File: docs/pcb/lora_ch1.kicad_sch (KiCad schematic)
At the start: 6 parts, among them J1 JST_02, U1 ESP32-C3_SUPERMINI_TH, U2 TP4056-42-ESOP8, U3 DRV2605LDGS, U4 AP2112K-3.3

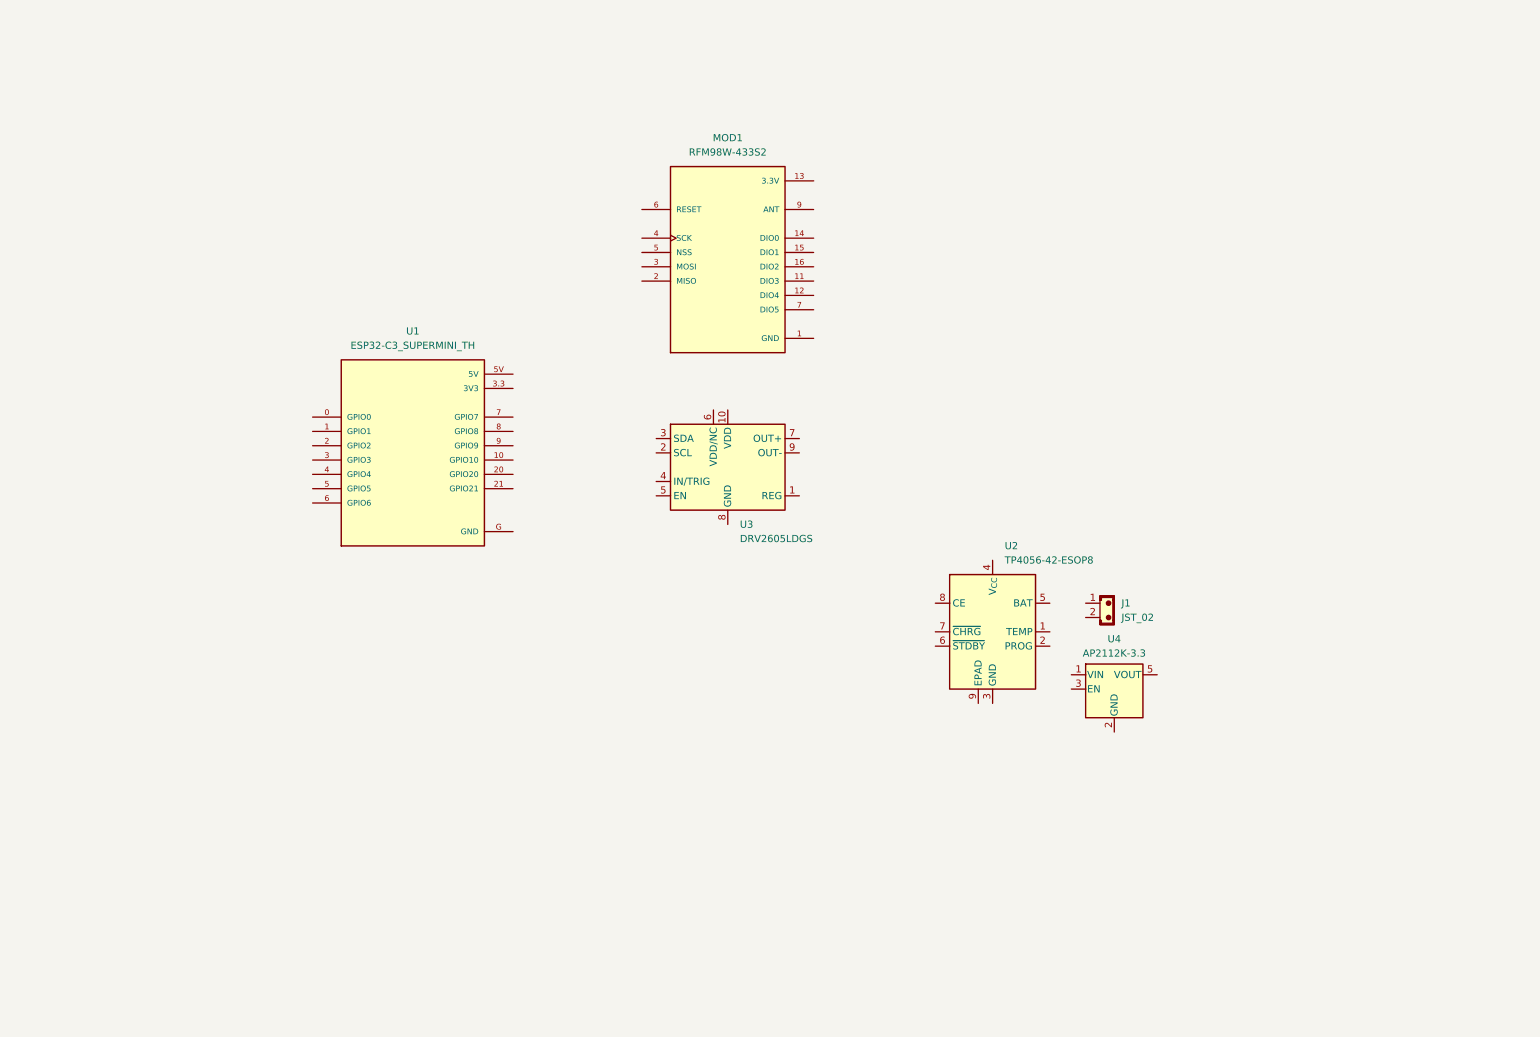
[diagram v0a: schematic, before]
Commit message: PCB schematic update, charging function added.
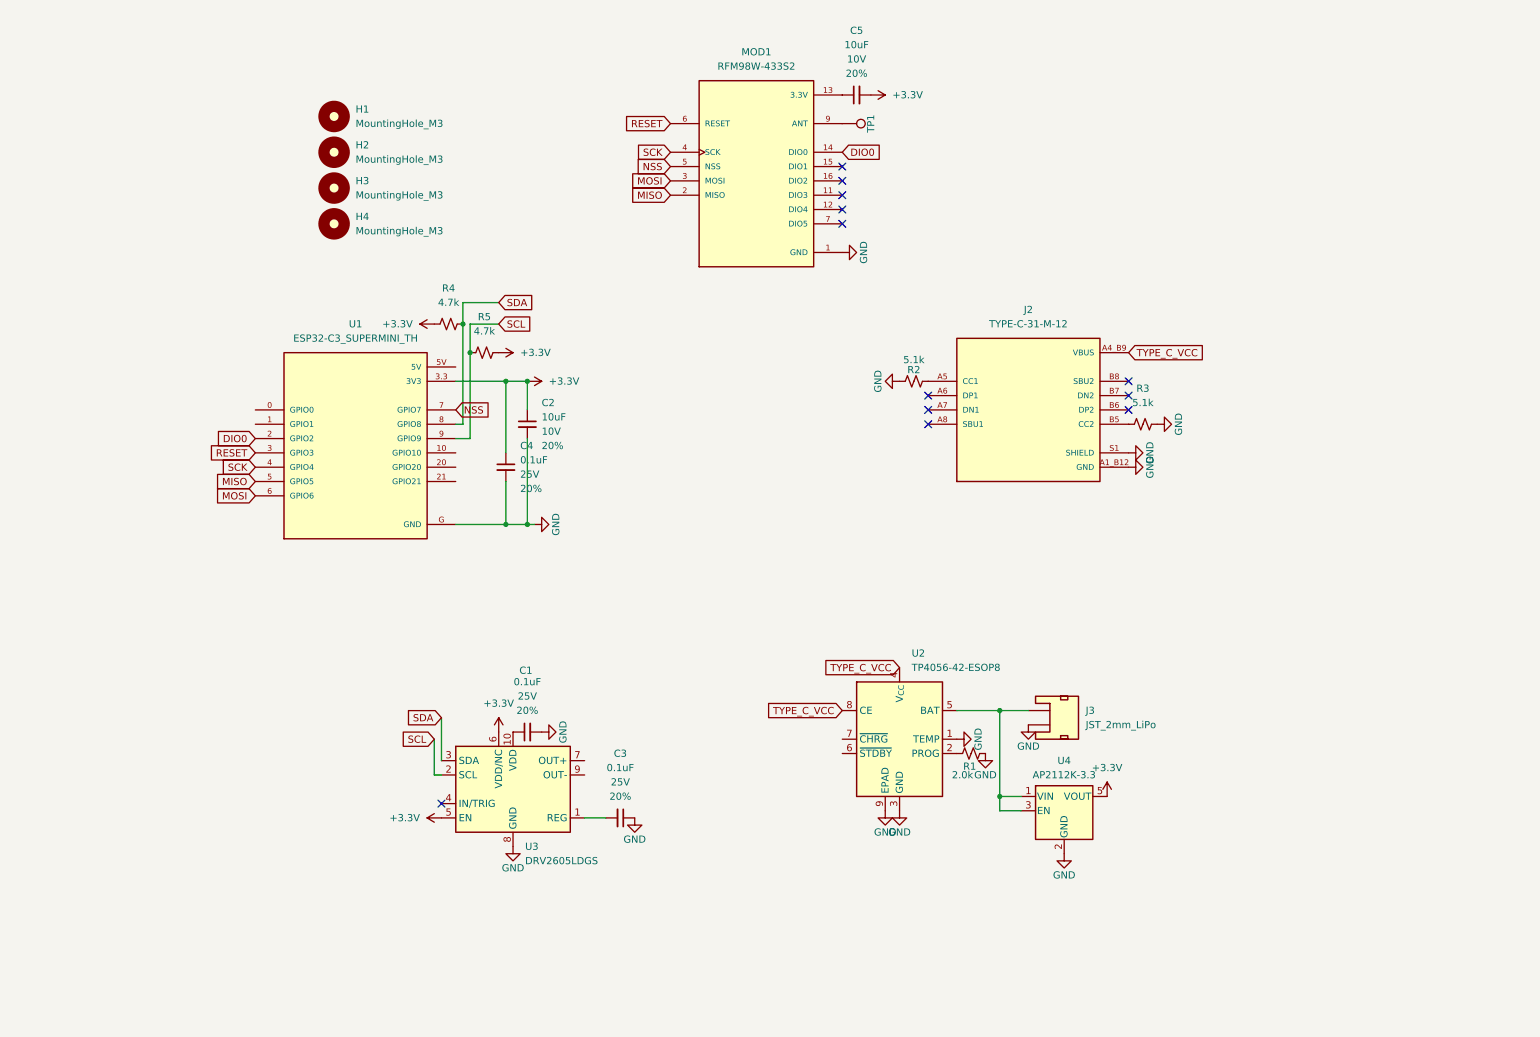
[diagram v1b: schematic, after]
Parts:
- removed J1: JST_02, Connector_JST:JST_EH_B2B-EH-A_1x02_P2.50mm_Vertical, symbol PCM_SL_Connectors:JST_02
- added C1, C3, C4: 0.1uF, PCM_SparkFun-Capacitor:C_0603_1608Metric, symbol PCM_SparkFun-Capacitor:0.1uF_0603_25V_20%
- added C2, C5: 10uF, PCM_SparkFun-Capacitor:C_0603_1608Metric, symbol PCM_SparkFun-Capacitor:10uF_0603_10V_20%
- added H1, H2, H3, H4: MountingHole_M3, MountingHole:MountingHole_3.2mm_M3, symbol PCM_SL_Mechanical:MountingHole_M3
- added J2: TYPE-C-31-M-12, TYPE-C-31-M-12:HRO_TYPE-C-31-M-12, symbol TYPE-C-31-M-12:TYPE-C-31-M-12
- added J3: JST_2mm_LiPo, PCM_SparkFun-Connector:JST_1x02_P2.0mm_Horizontal_SMD, symbol PCM_SparkFun-Connector:Conn_01x02_JST_P2.0mm_Horizontal_SMD
- added R1: 2.0k, PCM_SparkFun-Resistor:R_0603_1608Metric, symbol PCM_SparkFun-Resistor:2.0k_0603
- added R2, R3: 5.1k, PCM_SparkFun-Resistor:R_0603_1608Metric, symbol PCM_SparkFun-Resistor:5.1k_0603
- added R4, R5: 4.7k, PCM_SparkFun-Resistor:R_0603_1608Metric, symbol PCM_SparkFun-Resistor:4.7k_0603
- added TP1: 1.25mm, PCM_SparkFun-Connector:TestPoint-1.25mm, symbol PCM_SparkFun-Connector:TestPoint_1.25mm
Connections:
- net 3.3V: now also C5.1
- net GND: now also U1.G (GND), U2.1 (TEMP), U2.3 (GND), U2.9 (EPAD), U3.8 (GND), U4.2 (GND), C1.2, C2.2, C3.1, C4.2, J2.A1_B12 (GND), J2.B1_A12 (GND), J2.S1 (SHIELD), J2.S2 (SHIELD), J2.S3 (SHIELD), J2.S4 (SHIELD), J3.1 (-), R1.2, R2.1, R3.2
- net DIO0: now reaches MOD1.14 (DIO0), MOD1.14_1 (DIO0)
- net DIO0: now also U1.2 (GPIO2)
- net MISO: now reaches MOD1.2 (MISO), MOD1.2_1 (MISO)
- net MISO: now also U1.5 (GPIO5)
- net MOSI: now reaches MOD1.3 (MOSI), MOD1.3_1 (MOSI)
- net MOSI: now also U1.6 (GPIO6)
- net SCK: now reaches MOD1.4 (SCK), MOD1.4_1 (SCK)
- net SCK: now also U1.4 (GPIO4)
- net NSS: now reaches MOD1.5 (NSS), MOD1.5_1 (NSS)
- net NSS: now also U1.7 (GPIO7)
- net RESET: now reaches MOD1.6 (RESET), MOD1.6_1 (RESET)
- net RESET: now also U1.3 (GPIO3)
- net at MOD1.9 (ANT), MOD1.9_1 (ANT): now also TP1.1
- net at U4.1 (VIN): now also U2.5 (BAT), U4.3 (EN), J3.2 (+)
- net +3.3V: now reaches U4.5 (VOUT)
- net +3.3V: now also U1.3.3 (3V3), U3.5 (EN), U3.6 (VDD/NC), C2.1, C4.1, C5.2, R4.1, R5.2
- net at U2.2 (PROG): now also R1.1
- net VBUS: now reaches U2.4 (V_{CC})
- net VBUS: now also U2.8 (CE), J2.A4_B9 (VBUS), J2.B4_A9 (VBUS)
- net SDA: now reaches U1.8 (GPIO8)
- net SDA: now also U3.3 (SDA), R4.2
- net SCL: now reaches U1.9 (GPIO9)
- net SCL: now also U3.2 (SCL), R5.1
- net at U3.1 (REG): now also C3.2
- net at U3.10 (VDD): now also C1.1
- new net: J2.B5 (CC2), R3.1
- new net: J2.A5 (CC1), R2.2
- no-connect marks 0 -> 12
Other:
- moved on the sheet: MOD1, U1, U2, U3, U4

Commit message: PCB schematic finished.
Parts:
- removed C1, C3, C4: 0.1uF, PCM_SparkFun-Capacitor:C_0603_1608Metric, symbol PCM_SparkFun-Capacitor:0.1uF_0603_25V_20%
- removed J2: TYPE-C-31-M-12, TYPE-C-31-M-12:HRO_TYPE-C-31-M-12, symbol TYPE-C-31-M-12:TYPE-C-31-M-12
- removed J3: JST_2mm_LiPo, PCM_SparkFun-Connector:JST_1x02_P2.0mm_Horizontal_SMD, symbol PCM_SparkFun-Connector:Conn_01x02_JST_P2.0mm_Horizontal_SMD
- removed R3: 5.1k, PCM_SparkFun-Resistor:R_0603_1608Metric, symbol PCM_SparkFun-Resistor:5.1k_0603
- removed TP1: 1.25mm, PCM_SparkFun-Connector:TestPoint-1.25mm, symbol PCM_SparkFun-Connector:TestPoint_1.25mm
- removed U2: TP4056-42-ESOP8, Package_SO:SOIC-8-1EP_3.9x4.9mm_P1.27mm_EP2.41x3.3mm_ThermalVias, symbol Battery_Management:TP4056-42-ESOP8
- removed U3: DRV2605LDGS, Package_SO:VSSOP-10_3x3mm_P0.5mm, symbol Driver_Haptic:DRV2605LDGS
- removed U4: AP2112K-3.3, Package_TO_SOT_SMD:SOT-23-5, symbol Regulator_Linear:AP2112K-3.3
- added 3.3V_LDO1: XC6220B331MR, Package_TO_SOT_SMD:SOT-23-5, symbol Regulator_Linear:XC6220B331MR
- added ANT_PAD1, LRA+1, LRA-1: PINHD_1x1_Male, Connector_Pin:Pin_D1.0mm_L10.0mm_LooseFit, symbol PCM_SL_Pin_Headers:PINHD_1x1_Male
- added BATT_CON1: JST_2mm_LiPo, PCM_SparkFun-Connector:JST_1x02_P2.0mm_Horizontal_SMD, symbol PCM_SparkFun-Connector:Conn_01x02_JST_P2.0mm_Horizontal_SMD_LiPo
- added BATT_PROT1: DW01A, Package_TO_SOT_SMD:SOT-23-6, symbol Battery_Management:DW01A
- added BMS_FET1: FS8205A, FS8205A:SOP65P640X120-8N, symbol FS8205A:FS8205A
- added C1, C3, C4: 10uF, PCM_SparkFun-Capacitor:C_0603_1608Metric, symbol PCM_SparkFun-Capacitor:10uF_0603_10V_20%
- added C6: 100uF, PCM_SparkFun-Capacitor:C_1206_3216Metric, symbol PCM_SparkFun-Capacitor:100uF_1206_50V_10%
- added C7: 100nF, PCM_SparkFun-Capacitor:C_0603_1608Metric, symbol PCM_SparkFun-Capacitor:100uF_1206_50V_10%
- added C8: 1.0uF, PCM_SparkFun-Capacitor:C_0603_1608Metric, symbol PCM_SparkFun-Capacitor:1.0uF_0603_16V_10%
- added CHRG_MOD1: TP4056-42-ESOP8, Package_SO:SOIC-8-1EP_3.9x4.9mm_P1.27mm_EP2.41x3.3mm_ThermalVias, symbol Battery_Management:TP4056-42-ESOP8
- added D1: SS14, Diode_SMD:D_SMA, symbol Diode:SS14
- added INPT_BTN: Push_Button, Button_Switch_THT:SW_PUSH_6mm, symbol PCM_SL_Devices:Push_Button
- added LRA_DRV1: DRV2605LDGS, Package_SO:VSSOP-10_3x3mm_P0.5mm, symbol Driver_Haptic:DRV2605LDGS
- added Q1: AO3401A, Package_TO_SOT_SMD:SOT-23, symbol Transistor_FET:AO3401A
- added R10, R11, R3, R8: 100k, PCM_SparkFun-Resistor:R_0603_1608Metric, symbol PCM_SparkFun-Resistor:100k_0603
- added R6: 100, PCM_SparkFun-Resistor:R_0603_1608Metric, symbol PCM_SparkFun-Resistor:100_0603
- added R7: 1k, PCM_SparkFun-Resistor:R_0603_1608Metric, symbol PCM_SparkFun-Resistor:1k_0603
- added R9: 10k, PCM_SparkFun-Resistor:R_0603_1608Metric, symbol PCM_SparkFun-Resistor:10k_0603
- added TEST1: PINHD_1x6_Male, Connector_PinHeader_2.54mm:PinHeader_1x06_P2.54mm_Vertical, symbol PCM_SL_Pin_Headers:PINHD_1x6_Male
- C2, C5: LCSC (none) -> C19702
- R1: LCSC (none) -> C22975
- R4, R5: LCSC (none) -> C23162
- renumbered U1 to ESP32-C3-SUPERMINI1, MOD1 to LORA_MOD1, H1 to MOUNT1, H2 to MOUNT2, H3 to MOUNT3, H4 to MOUNT4
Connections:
- net NSS is gone; now on net LORA_NSS: ESP32-C3-SUPERMINI1.7 (GPIO7), LORA_MOD1.5 (NSS), LORA_MOD1.5_1 (NSS)
- net 3.3V: now also ESP32-C3-SUPERMINI1.3.3 (3V3), R2.1, R4.2, R5.1, 3.3V_LDO1.5 (VOUT), C1.2, C6.2, C7.1, TEST1.4; no longer C5.1
- net GND: now also C2.1, C5.1, R1.1, 3.3V_LDO1.2 (GND), BMS_FET1.6, BMS_FET1.7, C1.1, C3.1, C4.2, C6.1, C7.2, C8.2, CHRG_MOD1.1 (TEMP), CHRG_MOD1.3 (GND), INPT_BTN.1, LRA_DRV1.8 (GND), R10.1, R11.1, R3.2, R7.2, TEST1.1; no longer C2.2, R1.2, R2.1
- net SCL: now also R5.2, LRA_DRV1.2 (SCL), TEST1.3; no longer R5.1
- net SDA: now also R4.1, LRA_DRV1.3 (SDA), TEST1.2; no longer R4.2
- net ANT: now reaches LORA_MOD1.9 (ANT), LORA_MOD1.9_1 (ANT)
- net ANT: now also ANT_PAD1.1
- net at ESP32-C3-SUPERMINI1.0 (GPIO0): now also R3.1, R8.1
- net at ESP32-C3-SUPERMINI1.1 (GPIO1): now also INPT_BTN.2
- net LORA_DIO0: now reaches ESP32-C3-SUPERMINI1.10 (GPIO10)
- net LORA_DIO0: now also LORA_MOD1.14 (DIO0), LORA_MOD1.14_1 (DIO0), TEST1.6
- net CHRG: now reaches ESP32-C3-SUPERMINI1.20 (GPIO20)
- net CHRG: now also CHRG_MOD1.7 (~{CHRG})
- net DRV_EN: now reaches ESP32-C3-SUPERMINI1.21 (GPIO21)
- net V_USB: now reaches ESP32-C3-SUPERMINI1.5V
- net V_USB: now also C3.2, CHRG_MOD1.4 (V_{CC}), CHRG_MOD1.8 (CE), D1.2 (A), R9.1
- net LORA_NSS: now reaches R2.2
- removed net +3.3V: C2.1, C5.2, ESP32-C3-SUPERMINI1.3.3 (3V3), R4.1, R5.2
- removed net DIO0: ESP32-C3-SUPERMINI1.2 (GPIO2), LORA_MOD1.14 (DIO0), LORA_MOD1.14_1 (DIO0)
- net MISO renamed LORA_MISO
- net MOSI renamed LORA_MOSI
- net RESET renamed LORA_RST
- net SCK renamed LORA_SCK
- new net: Q1.1 (G), R10.2, R9.2
- new net: BATT_PROT1.5 (VCC), R6.2
- new net: BATT_PROT1.2 (CS), R7.1
- new net: CHRG_MOD1.2 (PROG), R1.2
- new net: BMS_FET1.1, BMS_FET1.8
- new net: C8.1, LRA_DRV1.1 (REG)
- new net DVR_EN: LRA_DRV1.5 (EN), R11.2
- new net LRA+: LRA+1.1, LRA_DRV1.7 (OUT+)
- new net LRA-: LRA-1.1, LRA_DRV1.9 (OUT-)
- new net OC: BATT_PROT1.3 (OC), BMS_FET1.5
- new net OD: BATT_PROT1.1 (OD), BMS_FET1.4
- new net VBAT+: BATT_CON1.2 (+), C4.1, CHRG_MOD1.5 (BAT), Q1.2 (S), R6.1, R8.2
- new net VBAT-: BATT_CON1.1 (-), BATT_PROT1.6 (GND), BMS_FET1.2, BMS_FET1.3
- new net V_IN: 3.3V_LDO1.1 (VIN), 3.3V_LDO1.3 (CE), C2.2, C5.2, D1.1 (K), LRA_DRV1.10 (VDD), LRA_DRV1.6 (VDD/NC), Q1.3 (D), TEST1.5
- no-connect marks 12 -> 8
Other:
- moved on the sheet: ESP32-C3-SUPERMINI1, LORA_MOD1, MOUNT1, MOUNT2, MOUNT3, MOUNT4

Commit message: PCB design finished.
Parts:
- added C10, C11, C9: 0.1uF, PCM_SparkFun-Capacitor:C_0603_1608Metric, symbol PCM_SparkFun-Capacitor:0.1uF_0603_25V_20%
- added R12: 10k, PCM_SparkFun-Resistor:R_0603_1608Metric, symbol PCM_SparkFun-Resistor:10k_0603
- C8: LCSC (none) -> C15849
- MOSFET1: renamed from Q1; LCSC (none) -> C15127
- R10, R11, R3, R8: LCSC (none) -> C25803
- R2: LCSC (none) -> C23186
- R9: LCSC (none) -> C25804
- SSD1: renamed from D1; LCSC (none) -> C2480
- renumbered INPT_BTN to INPT_BTN1
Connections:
- net DVR_EN is gone; now on net DRV_EN: LRA_DRV1.5 (EN), R11.2
- net 3.3V: now also R12.2
- net CHRG: now also R12.1
- net GND: now also CHRG_MOD1.9 (EPAD), C10.1, C11.2
- net V_IN: now also C11.1
- net at ESP32-C3-SUPERMINI1.0 (GPIO0), R3.1, R8.1: now also C10.2
- net at BATT_PROT1.5 (VCC), R6.2: now also C9.1
- net VBAT+ renamed BATT_PLUS
- net VBAT- renamed BATT_MINUS
- net BATT_MINUS: now also C9.2
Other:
- moved on the sheet: BATT_PROT1, R6, R7

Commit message: PCB ready to print.
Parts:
- removed ESP32-C3-SUPERMINI1: ESP32-C3_SUPERMINI_TH, ESP32-C3_SUPERMINI_TH:MODULE_ESP32-C3_SUPERMINI_TH, symbol ESP32-C3_SUPERMINI_TH:ESP32-C3_SUPERMINI_TH
- added ESP1: ESP32-C3_SUPERMINI_SMD, ESP32-C3_SUPERMINI_SMD:MODULE_ESP32-C3_SUPERMINI, symbol ESP32-C3_SUPERMINI_SMD:ESP32-C3_SUPERMINI_SMD
- BMS1: renamed from BMS_FET1; LCSC C2830320 -> C5148694
- C10, C11, C9: LCSC (none) -> C14663
- LORA1: renamed from LORA_MOD1; LCSC (none) -> C19078268
- renumbered ANT_PAD1 to ANT1, BATT_CON1 to BATTC1, BATT_PROT1 to BATTP1, CHRG_MOD1 to CHRG1, LRA_DRV1 to HAPTIC1, 3.3V_LDO1 to LDO1, LRA-1 to LRAM1, LRA+1 to LRAP1
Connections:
- net 3.3V: now also ESP1.3.3 (3V3)
- net CHRG: now also ESP1.20 (GPIO20)
- net DRV_EN: now also ESP1.21 (GPIO21)
- net GND: now also ESP1.G (GND)
- net LORA_DIO0: now also ESP1.10 (GPIO10)
- net LORA_MISO: now also ESP1.5 (GPIO5)
- net LORA_MOSI: now also ESP1.6 (GPIO6)
- net LORA_NSS: now also ESP1.7 (GPIO7)
- net LORA_RST: now also ESP1.3 (GPIO3)
- net LORA_SCK: now also ESP1.4 (GPIO4)
- net SCL: now also ESP1.9 (GPIO9)
- net SDA: now also ESP1.8 (GPIO8)
- net V_USB: now also ESP1.5V
- net at C10.2, R3.1, R8.1: now also ESP1.0 (GPIO0)
- net at INPT_BTN1.2: now also ESP1.1 (GPIO1)
